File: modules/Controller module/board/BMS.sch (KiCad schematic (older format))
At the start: 16 parts, among them IC1 DW01A, J6 Conn_01x02_Female, Q3 AO3401A, Q4 FS8205A, U4 TP4056

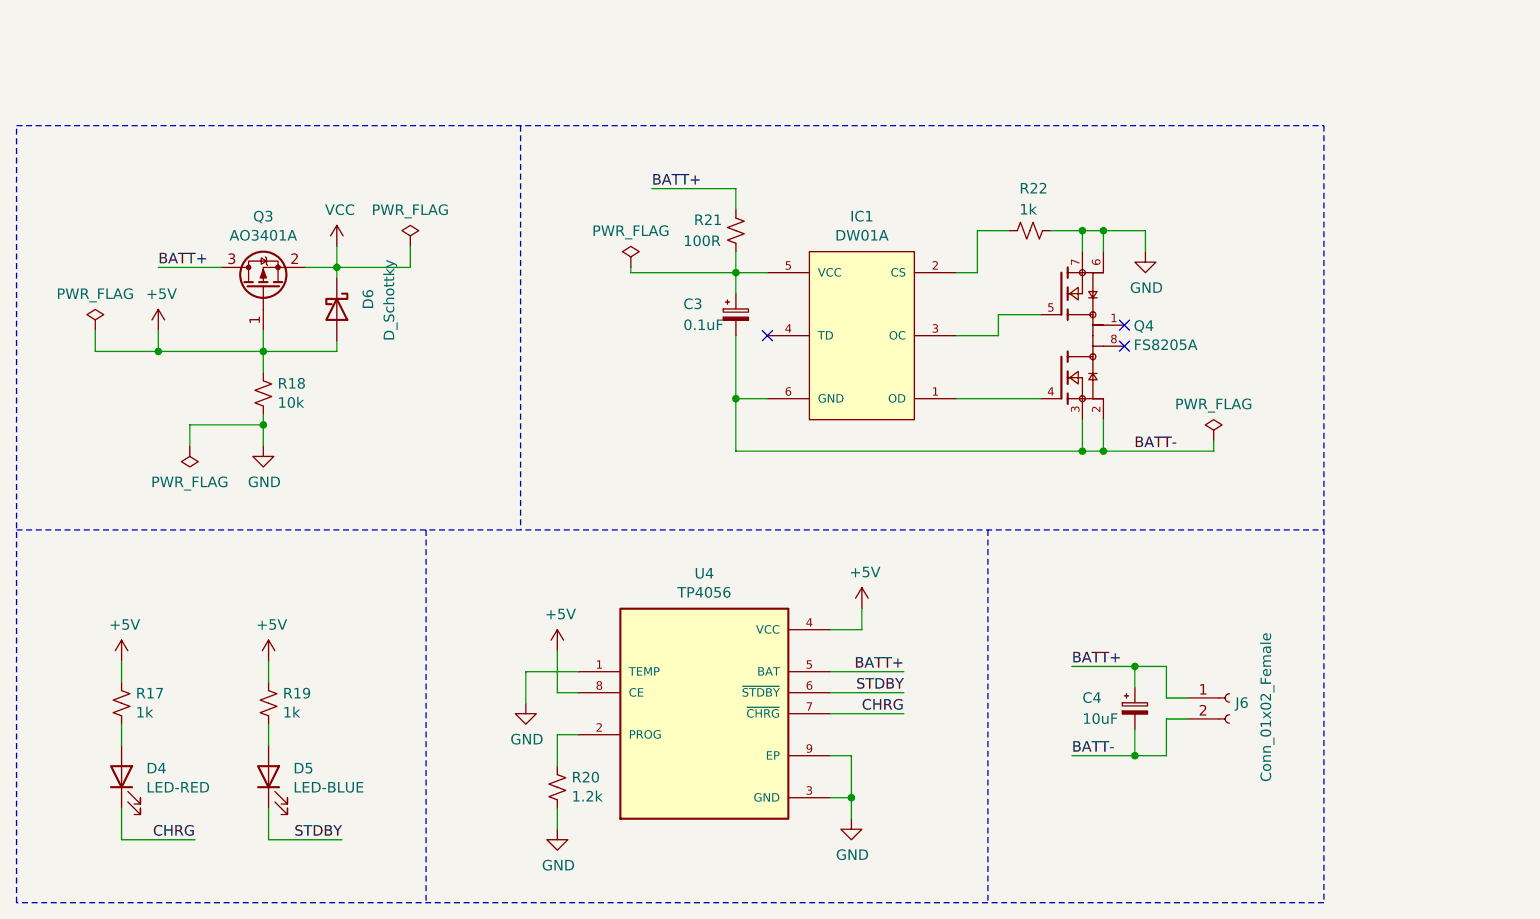
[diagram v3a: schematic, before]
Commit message: PCB: IMU
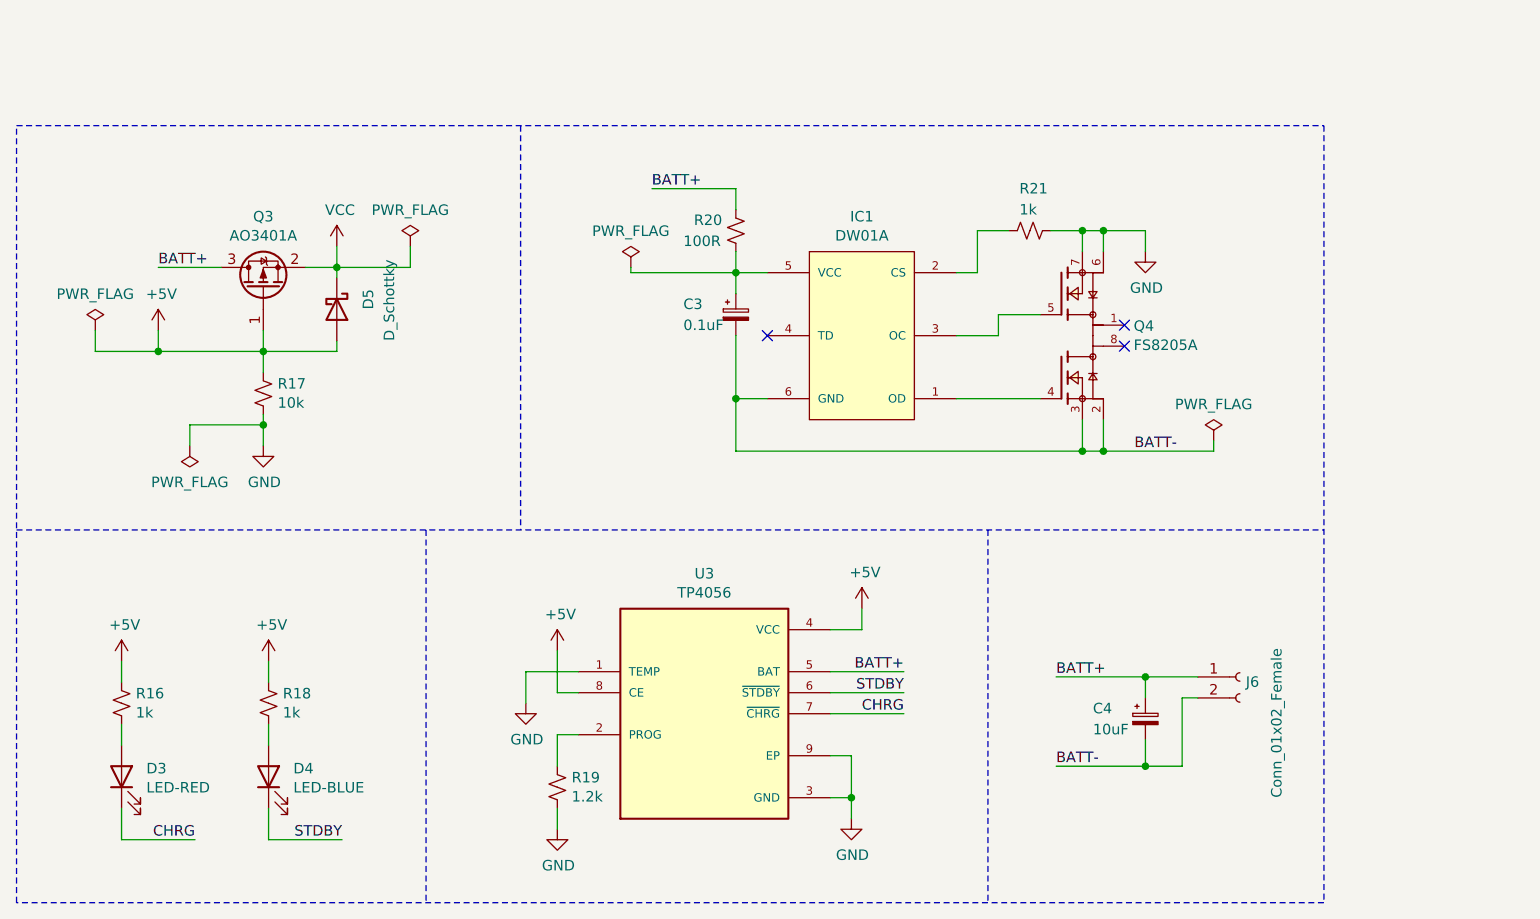
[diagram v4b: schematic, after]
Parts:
- renumbered D4 to D3, D5 to D4, D6 to D5, R17 to R16, R18 to R17, R19 to R18, R20 to R19, R21 to R20, R22 to R21, U4 to U3
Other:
- moved on the sheet: C4, J6
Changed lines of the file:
@@
 $Descr A4 11693 8268
 encoding utf-8
-Sheet 2 2
+Sheet 2 3
 Title ""
 Date ""
@@
 $EndDescr
 $Comp
-L Device:R_Small_US R17
+L Device:R_Small_US R16
 U 1 1 619958ED
 P 2975 4425
-F 0 "R17" H 3043 4471 50  0000 L CNN
+F 0 "R16" H 3043 4471 50  0000 L CNN
 F 1 "1k" H 3043 4380 50  0000 L CNN
 F 2 "Resistor_SMD:R_0805_2012Metric_Pad1.20x1.40mm_HandSolder" H 2975 4425 50  0001 C CNN
@@
 $EndComp
 $Comp
-L Device:LED D4
+L Device:LED D3
 U 1 1 61995CCB
 P 2975 4775
-F 0 "D4" V 3014 4657 50  0000 R CNN
+F 0 "D3" V 3014 4657 50  0000 R CNN
 F 1 "LED-RED" V 2923 4657 50  0000 R CNN
 F 2 "LED_SMD:LED_0805_2012Metric_Pad1.15x1.40mm_HandSolder" H 2975 4775 50  0001 C CNN
@@
 	2975 4525 2975 4625
 $Comp
-L Device:R_Small_US R19
+L Device:R_Small_US R18
 U 1 1 619979BF
 P 3675 4425
-F 0 "R19" H 3743 4471 50  0000 L CNN
+F 0 "R18" H 3743 4471 50  0000 L CNN
 F 1 "1k" H 3743 4380 50  0000 L CNN
 F 2 "Resistor_SMD:R_0805_2012Metric_Pad1.20x1.40mm_HandSolder" H 3675 4425 50  0001 C CNN
@@
 $EndComp
 $Comp
-L Device:LED D5
+L Device:LED D4
 U 1 1 619979C5
 P 3675 4775
-F 0 "D5" V 3714 4657 50  0000 R CNN
+F 0 "D4" V 3714 4657 50  0000 R CNN
 F 1 "LED-BLUE" V 3623 4657 50  0000 R CNN
 F 2 "LED_SMD:LED_0805_2012Metric_Pad1.15x1.40mm_HandSolder" H 3675 4775 50  0001 C CNN
@@
 Text Label 4025 5075 2    50   ~ 0
 STDBY
-Text Label 7500 4250 0    50   ~ 0
-BATT+
 Wire Wire Line
 	7850 2175 7850 2275
 $Comp
-L power:GND #PWR041
+L power:GND #PWR038
 U 1 1 619B7FBD
 P 7850 2275
-F 0 "#PWR041" H 7850 2025 50  0001 C CNN
+F 0 "#PWR038" H 7850 2025 50  0001 C CNN
 F 1 "GND" H 7855 2102 50  0000 C CNN
 F 2 "" H 7850 2275 50  0001 C CNN
@@
 	1    0    0    -1
 $EndComp
-Wire Wire Line
-	7500 4250 7800 4250
-$Comp
-L Device:CP_Small C4
-U 1 1 619B9D05
-P 7800 4450
-F 0 "C4" H 7550 4500 50  0000 L CNN
-F 1 "10uF" H 7550 4400 50  0000 L CNN
-F 2 "Capacitor_SMD:C_0805_2012Metric_Pad1.18x1.45mm_HandSolder" H 7800 4450 50  0001 C CNN
-F 3 "~" H 7800 4450 50  0001 C CNN
-	1    7800 4450
-	1    0    0    -1
-$EndComp
-Wire Wire Line
-	7800 4350 7800 4250
 $Comp
 L Transistor_FET:AO3401A Q3
@@
 $EndComp
 $Comp
-L Device:D_Schottky D6
+L Device:D_Schottky D5
 U 1 1 61A4897E
 P 4000 2550
-F 0 "D6" H 4000 2700 50  0000 R CNN
+F 0 "D5" H 4000 2700 50  0000 R CNN
 F 1 "D_Schottky" H 4150 2800 50  0000 R CNN
 F 2 "Diode_SMD:D_SMA" H 4000 2550 50  0001 C CNN
@@
 $EndComp
 $Comp
-L Device:R_Small_US R18
+L Device:R_Small_US R17
 U 1 1 61A4EED8
 P 3650 2950
-F 0 "R18" H 3718 2996 50  0000 L CNN
+F 0 "R17" H 3718 2996 50  0000 L CNN
 F 1 "10k" H 3718 2905 50  0000 L CNN
 F 2 "Resistor_SMD:R_0805_2012Metric_Pad1.20x1.40mm_HandSolder" H 3650 2950 50  0001 C CNN
@@
 $EndComp
 $Comp
-L power:GND #PWR033
+L power:GND #PWR030
 U 1 1 61A4FE63
 P 3650 3200
-F 0 "#PWR033" H 3650 2950 50  0001 C CNN
+F 0 "#PWR030" H 3650 2950 50  0001 C CNN
 F 1 "GND" H 3655 3027 50  0000 C CNN
 F 2 "" H 3650 3200 50  0001 C CNN
@@
 	3150 2750 3650 2750
 $Comp
-L power:+5V #PWR032
+L power:+5V #PWR029
 U 1 1 61A68B7A
 P 3150 2650
-F 0 "#PWR032" H 3150 2500 50  0001 C CNN
+F 0 "#PWR029" H 3150 2500 50  0001 C CNN
 F 1 "+5V" H 3165 2823 50  0000 C CNN
 F 2 "" H 3150 2650 50  0001 C CNN
@@
 	3150 2650 3150 2750
 $Comp
-L power:VCC #PWR035
+L power:VCC #PWR032
 U 1 1 61A6A8F1
 P 4000 2250
-F 0 "#PWR035" H 4000 2100 50  0001 C CNN
+F 0 "#PWR032" H 4000 2100 50  0001 C CNN
 F 1 "VCC" H 4015 2423 50  0000 C CNN
 F 2 "" H 4000 2250 50  0001 C CNN
@@
 Wire Wire Line
 	7650 2175 7850 2175
-Text Label 7500 4675 0    50   ~ 0
-BATT-
-Wire Wire Line
-	7500 4675 7800 4675
-Wire Wire Line
-	7800 4550 7800 4675
-$Comp
-L Connector:Conn_01x02_Female J6
-U 1 1 619B0A12
-P 8250 4400
-F 0 "J6" H 8278 4376 50  0000 L CNN
-F 1 "Conn_01x02_Female" V 8425 4000 50  0000 L CNN
-F 2 "Board:SolderWire_1x02_P2.00mm" H 8250 4400 50  0001 C CNN
-F 3 "~" H 8250 4400 50  0001 C CNN
-	1    8250 4400
-	1    0    0    -1
-$EndComp
-Wire Wire Line
-	7800 4250 7950 4250
-Wire Wire Line
-	7950 4400 8050 4400
-Connection ~ 7800 4250
-Wire Wire Line
-	8050 4500 7950 4500
-Wire Wire Line
-	7950 4675 7800 4675
 Text Label 8000 3225 2    50   ~ 0
 BATT-
@@
 Connection ~ 7650 3225
 $Comp
-L Device:R_Small_US R21
+L Device:R_Small_US R20
 U 1 1 61A90319
 P 5900 2175
-F 0 "R21" H 5700 2225 50  0000 L CNN
+F 0 "R20" H 5700 2225 50  0000 L CNN
 F 1 "100R" H 5650 2125 50  0000 L CNN
 F 2 "Resistor_SMD:R_0805_2012Metric_Pad1.20x1.40mm_HandSolder" H 5900 2175 50  0001 C CNN
@@
 	5900 1975 5900 2075
 $Comp
-L Device:R_Small_US R22
+L Device:R_Small_US R21
 U 1 1 61A9D27D
 P 7300 2175
-F 0 "R22" V 7100 2125 50  0000 L CNN
+F 0 "R21" V 7100 2125 50  0000 L CNN
 F 1 "1k" V 7200 2125 50  0000 L CNN
 F 2 "Resistor_SMD:R_0805_2012Metric_Pad1.20x1.40mm_HandSolder" H 7300 2175 50  0001 C CNN
@@
 Connection ~ 7550 3225
 $Comp
-L power:+5V #PWR031
+L power:+5V #PWR028
 U 1 1 61B45860
 P 2975 4225
-F 0 "#PWR031" H 2975 4075 50  0001 C CNN
+F 0 "#PWR028" H 2975 4075 50  0001 C CNN
 F 1 "+5V" H 2990 4398 50  0000 C CNN
 F 2 "" H 2975 4225 50  0001 C CNN
@@
 $EndComp
 $Comp
-L power:+5V #PWR034
+L power:+5V #PWR031
 U 1 1 61B45E6A
 P 3675 4225
-F 0 "#PWR034" H 3675 4075 50  0001 C CNN
+F 0 "#PWR031" H 3675 4075 50  0001 C CNN
 F 1 "+5V" H 3690 4398 50  0000 C CNN
 F 2 "" H 3675 4225 50  0001 C CNN
@@
 $EndComp
 $Comp
-L power:PWR_FLAG #FLG04
+L power:PWR_FLAG #FLG03
 U 1 1 621A8DAA
 P 4350 2250
-F 0 "#FLG04" H 4350 2325 50  0001 C CNN
+F 0 "#FLG03" H 4350 2325 50  0001 C CNN
 F 1 "PWR_FLAG" H 4350 2423 50  0000 C CNN
 F 2 "" H 4350 2250 50  0001 C CNN
@@
 	4000 2350 4350 2350
 $Comp
-L power:PWR_FLAG #FLG02
+L power:PWR_FLAG #FLG01
 U 1 1 621ACEAA
 P 2850 2650
-F 0 "#FLG02" H 2850 2725 50  0001 C CNN
+F 0 "#FLG01" H 2850 2725 50  0001 C CNN
 F 1 "PWR_FLAG" H 2850 2823 50  0000 C CNN
 F 2 "" H 2850 2650 50  0001 C CNN
@@
 $EndComp
 $Comp
-L power:PWR_FLAG #FLG03
+L power:PWR_FLAG #FLG02
 U 1 1 621AD5F9
 P 3300 3200
-F 0 "#FLG03" H 3300 3275 50  0001 C CNN
+F 0 "#FLG02" H 3300 3275 50  0001 C CNN
 F 1 "PWR_FLAG" H 3300 3373 50  0000 C CNN
 F 2 "" H 3300 3200 50  0001 C CNN
@@
 Connection ~ 3650 3100
 $Comp
-L power:PWR_FLAG #FLG05
+L power:PWR_FLAG #FLG04
 U 1 1 621B6BD1
 P 5400 2350
-F 0 "#FLG05" H 5400 2425 50  0001 C CNN
+F 0 "#FLG04" H 5400 2425 50  0001 C CNN
 F 1 "PWR_FLAG" H 5400 2523 50  0000 C CNN
 F 2 "" H 5400 2350 50  0001 C CNN
@@
 	5400 2375 5900 2375
 $Comp
-L power:PWR_FLAG #FLG06
+L power:PWR_FLAG #FLG05
 U 1 1 621B97BA
 P 8175 3175
-F 0 "#FLG06" H 8175 3250 50  0001 C CNN
+F 0 "#FLG05" H 8175 3250 50  0001 C CNN
 F 1 "PWR_FLAG" H 8175 3348 50  0000 C CNN
 F 2 "" H 8175 3175 50  0001 C CNN
@@
 Wire Wire Line
 	7650 3225 8175 3225
-Wire Wire Line
-	7950 4250 7950 4400
-Wire Wire Line
-	7950 4500 7950 4675
-Connection ~ 7800 4675
-$Comp
-L power:+5V #PWR040
+$Comp
+L power:+5V #PWR037
 U 1 1 61B44D3F
 P 6500 3975
-F 0 "#PWR040" H 6500 3825 50  0001 C CNN
+F 0 "#PWR037" H 6500 3825 50  0001 C CNN
 F 1 "+5V" H 6515 4148 50  0000 C CNN
 F 2 "" H 6500 3975 50  0001 C CNN
@@
 $EndComp
 $Comp
-L power:+5V #PWR037
+L power:+5V #PWR034
 U 1 1 61B44133
 P 5050 4175
-F 0 "#PWR037" H 5050 4025 50  0001 C CNN
+F 0 "#PWR034" H 5050 4025 50  0001 C CNN
 F 1 "+5V" H 5065 4348 50  0000 C CNN
 F 2 "" H 5050 4175 50  0001 C CNN
@@
 	6350 4275 6700 4275
 $Comp
-L power:GND #PWR039
+L power:GND #PWR036
 U 1 1 619A0A50
 P 6450 4975
-F 0 "#PWR039" H 6450 4725 50  0001 C CNN
+F 0 "#PWR036" H 6450 4725 50  0001 C CNN
 F 1 "GND" H 6455 4802 50  0000 C CNN
 F 2 "" H 6450 4975 50  0001 C CNN
@@
 	5050 4925 5050 5025
 $Comp
-L Device:R_Small_US R20
+L Device:R_Small_US R19
 U 1 1 6199F776
 P 5050 4825
-F 0 "R20" H 5118 4871 50  0000 L CNN
+F 0 "R19" H 5118 4871 50  0000 L CNN
 F 1 "1.2k" H 5118 4780 50  0000 L CNN
 F 2 "Resistor_SMD:R_0805_2012Metric_Pad1.20x1.40mm_HandSolder" H 5050 4825 50  0001 C CNN
@@
 $EndComp
 $Comp
-L power:GND #PWR038
+L power:GND #PWR035
 U 1 1 6199F212
 P 5050 5025
-F 0 "#PWR038" H 5050 4775 50  0001 C CNN
+F 0 "#PWR035" H 5050 4775 50  0001 C CNN
 F 1 "GND" H 5055 4852 50  0000 C CNN
 F 2 "" H 5050 5025 50  0001 C CNN
@@
 	5050 4175 5050 4375
 $Comp
-L TP4056:TP4056 U4
+L TP4056:TP4056 U3
 U 1 1 61994B2B
 P 5750 4475
-F 0 "U4" H 5750 5142 50  0000 C CNN
+F 0 "U3" H 5750 5142 50  0000 C CNN
 F 1 "TP4056" H 5750 5051 50  0000 C CNN
 F 2 "Board:SOP127P600X175-9N" H 5750 4475 50  0001 L BNN
@@
 	5150 4575 5050 4575
 $Comp
-L power:GND #PWR036
+L power:GND #PWR033
 U 1 1 6199BAE9
 P 4900 4425
-F 0 "#PWR036" H 4900 4175 50  0001 C CNN
+F 0 "#PWR033" H 4900 4175 50  0001 C CNN
 F 1 "GND" H 4905 4252 50  0000 C CNN
 F 2 "" H 4900 4425 50  0001 C CNN
@@
 Wire Notes Line
 	7100 3600 7100 5375
+$Comp
+L Connector:Conn_01x02_Female J6
+U 1 1 619B0A12
+P 8300 4300
+F 0 "J6" H 8328 4276 50  0000 L CNN
+F 1 "Conn_01x02_Female" V 8475 3725 50  0000 L CNN
+F 2 "Board:SolderWire_1x02_P2.00mm" H 8300 4300 50  0001 C CNN
+F 3 "~" H 8300 4300 50  0001 C CNN
+	1    8300 4300
+	1    0    0    -1
+$EndComp
+Wire Wire Line
+	7850 4600 7850 4725
+Text Label 7425 4725 0    50   ~ 0
+BATT-
+Wire Wire Line
+	7850 4400 7850 4300
+$Comp
+L Device:CP_Small C4
+U 1 1 619B9D05
+P 7850 4500
+F 0 "C4" H 7600 4550 50  0000 L CNN
+F 1 "10uF" H 7600 4450 50  0000 L CNN
+F 2 "Capacitor_SMD:C_0805_2012Metric_Pad1.18x1.45mm_HandSolder" H 7850 4500 50  0001 C CNN
+F 3 "~" H 7850 4500 50  0001 C CNN
+	1    7850 4500
+	1    0    0    -1
+$EndComp
+Text Label 7425 4300 0    50   ~ 0
+BATT+
+Wire Wire Line
+	7850 4300 8100 4300
+Wire Wire Line
+	8100 4400 8025 4400
+Wire Wire Line
+	8025 4400 8025 4725
+Wire Wire Line
+	7850 4725 8025 4725
+Wire Wire Line
+	7425 4300 7850 4300
+Connection ~ 7850 4300
+Wire Wire Line
+	7425 4725 7850 4725
+Connection ~ 7850 4725
 $EndSCHEMATC

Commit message: Controller module: Optical Flow Sensor Connector
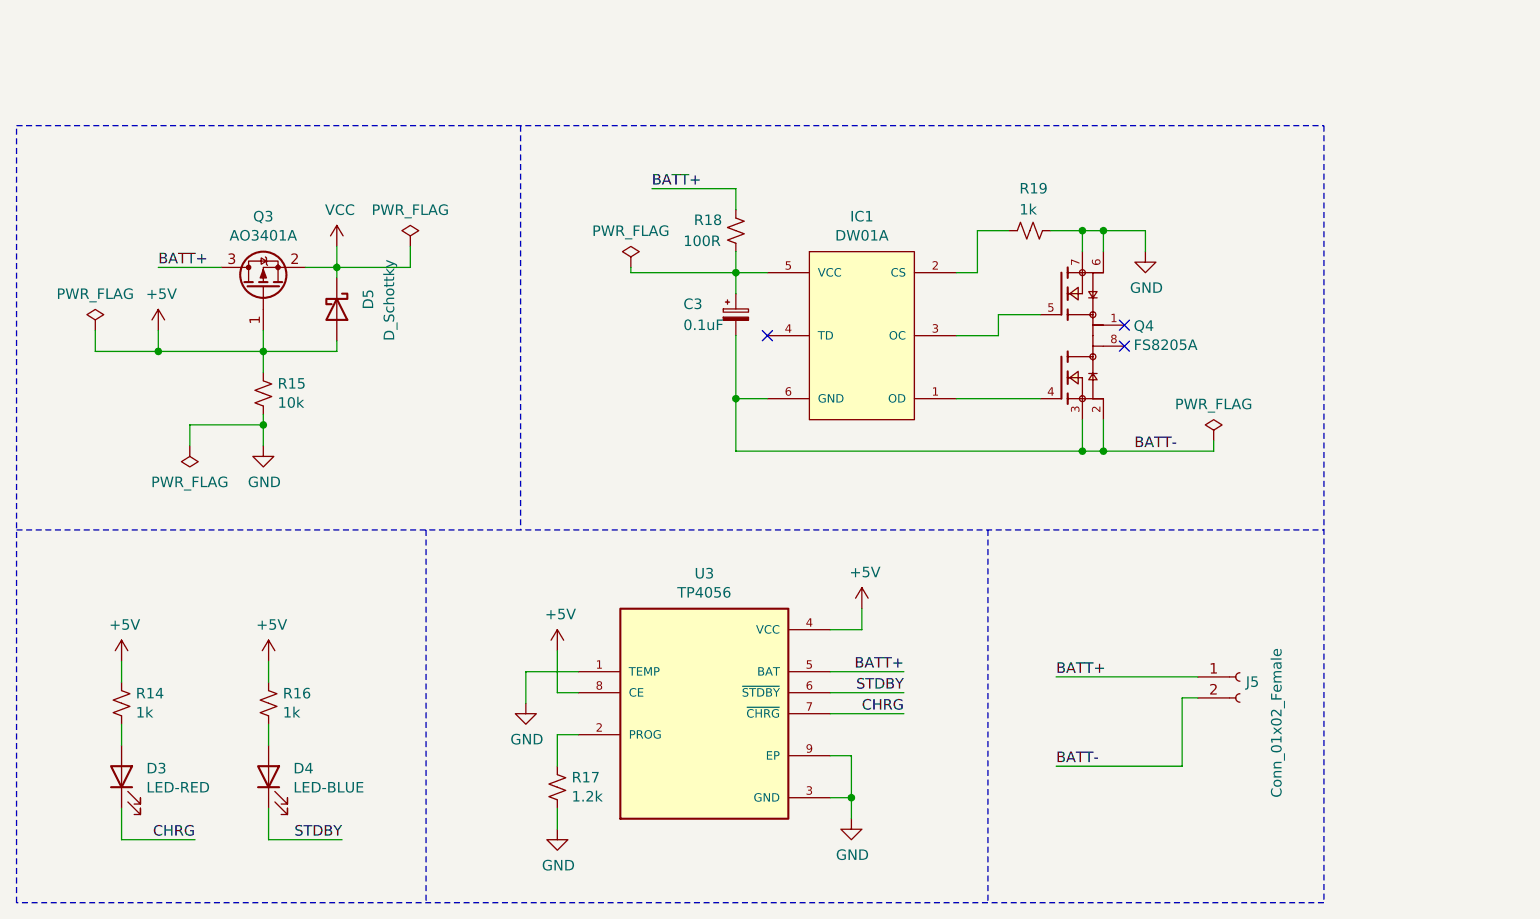
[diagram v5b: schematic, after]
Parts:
- removed C4: 10uF, Capacitor_SMD:C_0805_2012Metric_Pad1.18x1.45mm_HandSolder, symbol Device:CP_Small
- renumbered J6 to J5, R16 to R14, R17 to R15, R18 to R16, R19 to R17, R20 to R18, R21 to R19
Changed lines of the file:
@@
 $Descr A4 11693 8268
 encoding utf-8
-Sheet 2 3
+Sheet 2 4
 Title ""
 Date ""
@@
 $EndDescr
 $Comp
-L Device:R_Small_US R16
+L Device:R_Small_US R14
 U 1 1 619958ED
 P 2975 4425
-F 0 "R16" H 3043 4471 50  0000 L CNN
+F 0 "R14" H 3043 4471 50  0000 L CNN
 F 1 "1k" H 3043 4380 50  0000 L CNN
 F 2 "Resistor_SMD:R_0805_2012Metric_Pad1.20x1.40mm_HandSolder" H 2975 4425 50  0001 C CNN
@@
 	2975 4525 2975 4625
 $Comp
-L Device:R_Small_US R18
+L Device:R_Small_US R16
 U 1 1 619979BF
 P 3675 4425
-F 0 "R18" H 3743 4471 50  0000 L CNN
+F 0 "R16" H 3743 4471 50  0000 L CNN
 F 1 "1k" H 3743 4380 50  0000 L CNN
 F 2 "Resistor_SMD:R_0805_2012Metric_Pad1.20x1.40mm_HandSolder" H 3675 4425 50  0001 C CNN
@@
 $EndComp
 $Comp
-L Device:R_Small_US R17
+L Device:R_Small_US R15
 U 1 1 61A4EED8
 P 3650 2950
-F 0 "R17" H 3718 2996 50  0000 L CNN
+F 0 "R15" H 3718 2996 50  0000 L CNN
 F 1 "10k" H 3718 2905 50  0000 L CNN
 F 2 "Resistor_SMD:R_0805_2012Metric_Pad1.20x1.40mm_HandSolder" H 3650 2950 50  0001 C CNN
@@
 Connection ~ 7650 3225
 $Comp
-L Device:R_Small_US R20
+L Device:R_Small_US R18
 U 1 1 61A90319
 P 5900 2175
-F 0 "R20" H 5700 2225 50  0000 L CNN
+F 0 "R18" H 5700 2225 50  0000 L CNN
 F 1 "100R" H 5650 2125 50  0000 L CNN
 F 2 "Resistor_SMD:R_0805_2012Metric_Pad1.20x1.40mm_HandSolder" H 5900 2175 50  0001 C CNN
@@
 	5900 1975 5900 2075
 $Comp
-L Device:R_Small_US R21
+L Device:R_Small_US R19
 U 1 1 61A9D27D
 P 7300 2175
-F 0 "R21" V 7100 2125 50  0000 L CNN
+F 0 "R19" V 7100 2125 50  0000 L CNN
 F 1 "1k" V 7200 2125 50  0000 L CNN
 F 2 "Resistor_SMD:R_0805_2012Metric_Pad1.20x1.40mm_HandSolder" H 7300 2175 50  0001 C CNN
@@
 	5050 4925 5050 5025
 $Comp
-L Device:R_Small_US R19
+L Device:R_Small_US R17
 U 1 1 6199F776
 P 5050 4825
-F 0 "R19" H 5118 4871 50  0000 L CNN
+F 0 "R17" H 5118 4871 50  0000 L CNN
 F 1 "1.2k" H 5118 4780 50  0000 L CNN
 F 2 "Resistor_SMD:R_0805_2012Metric_Pad1.20x1.40mm_HandSolder" H 5050 4825 50  0001 C CNN
@@
 	7100 3600 7100 5375
 $Comp
-L Connector:Conn_01x02_Female J6
+L Connector:Conn_01x02_Female J5
 U 1 1 619B0A12
 P 8300 4300
-F 0 "J6" H 8328 4276 50  0000 L CNN
+F 0 "J5" H 8328 4276 50  0000 L CNN
 F 1 "Conn_01x02_Female" V 8475 3725 50  0000 L CNN
 F 2 "Board:SolderWire_1x02_P2.00mm" H 8300 4300 50  0001 C CNN
@@
 	1    0    0    -1
 $EndComp
-Wire Wire Line
-	7850 4600 7850 4725
 Text Label 7425 4725 0    50   ~ 0
 BATT-
-Wire Wire Line
-	7850 4400 7850 4300
-$Comp
-L Device:CP_Small C4
-U 1 1 619B9D05
-P 7850 4500
-F 0 "C4" H 7600 4550 50  0000 L CNN
-F 1 "10uF" H 7600 4450 50  0000 L CNN
-F 2 "Capacitor_SMD:C_0805_2012Metric_Pad1.18x1.45mm_HandSolder" H 7850 4500 50  0001 C CNN
-F 3 "~" H 7850 4500 50  0001 C CNN
-	1    7850 4500
-	1    0    0    -1
-$EndComp
 Text Label 7425 4300 0    50   ~ 0
 BATT+
 Wire Wire Line
-	7850 4300 8100 4300
-Wire Wire Line
 	8100 4400 8025 4400
 Wire Wire Line
 	8025 4400 8025 4725
 Wire Wire Line
-	7850 4725 8025 4725
-Wire Wire Line
-	7425 4300 7850 4300
-Connection ~ 7850 4300
-Wire Wire Line
-	7425 4725 7850 4725
-Connection ~ 7850 4725
+	7425 4725 8025 4725
+Wire Wire Line
+	7425 4300 8100 4300
 $EndSCHEMATC
